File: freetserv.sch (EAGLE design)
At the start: 60 parts, among them IC2 SN75240PW, Q1 12MHz, Q2 6MHz, U1 MCP16311-E/MS, U4 TLV810SDBZT, U5 SN74LVC1G86DCKR

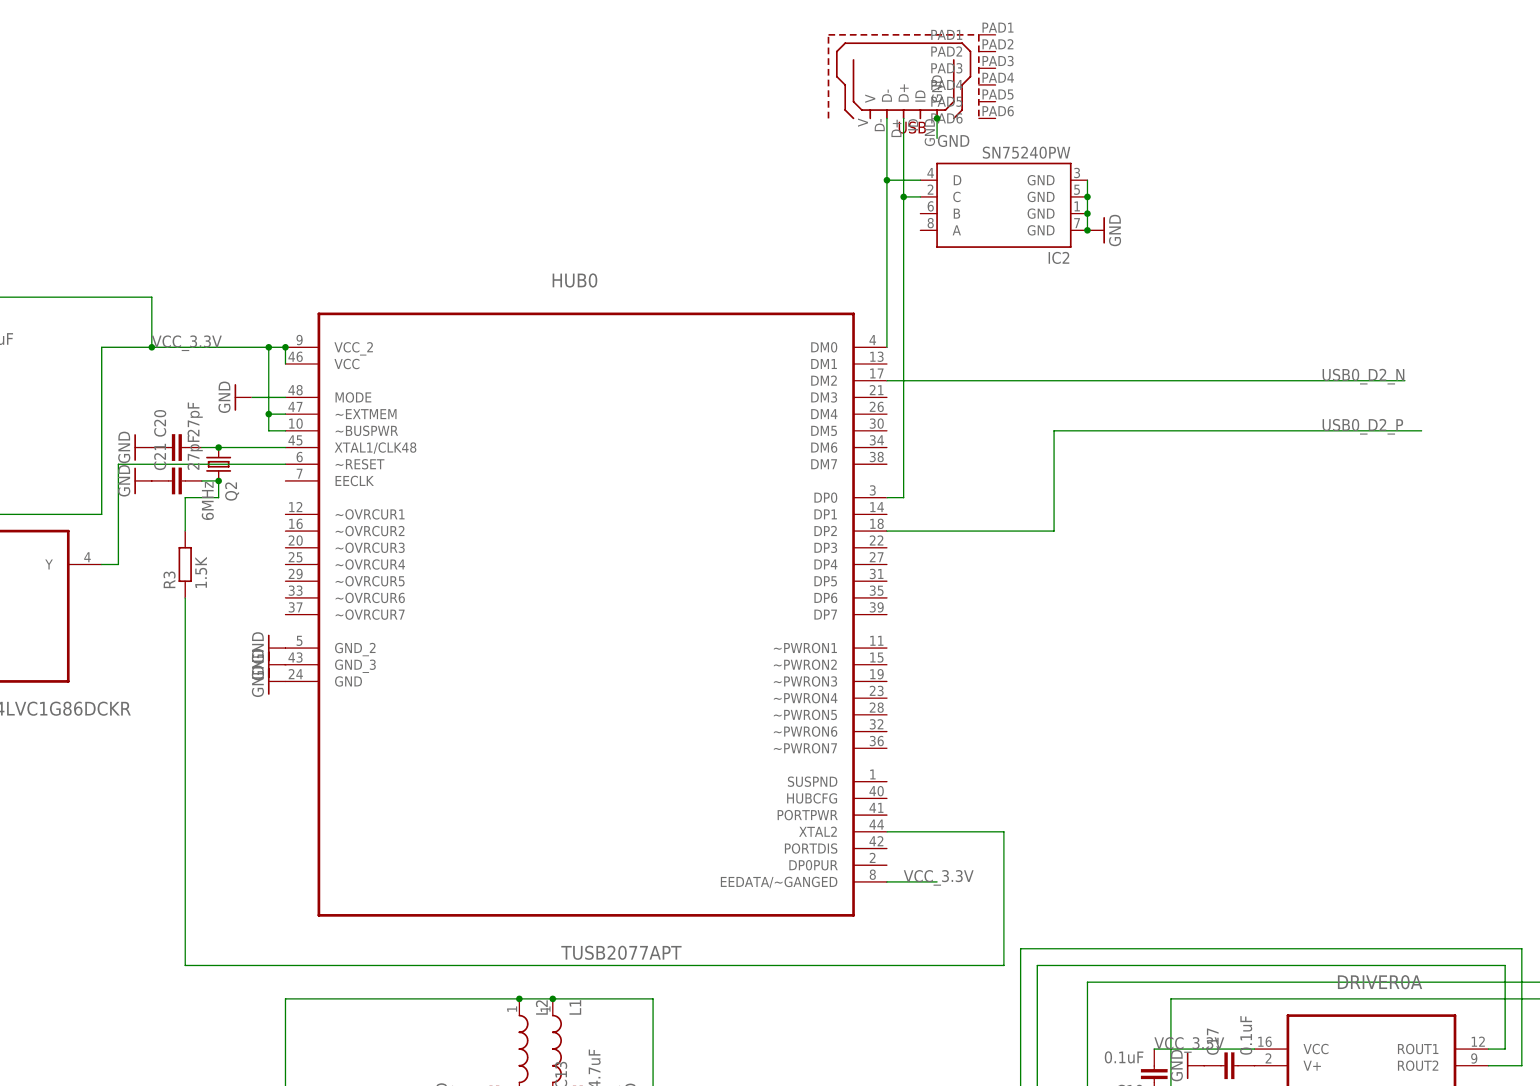
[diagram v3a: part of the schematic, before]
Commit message: use TUSB2046B (+ additional USB port), route both
Warnings need to be addressed, but the bulk of the routing should now be
done.
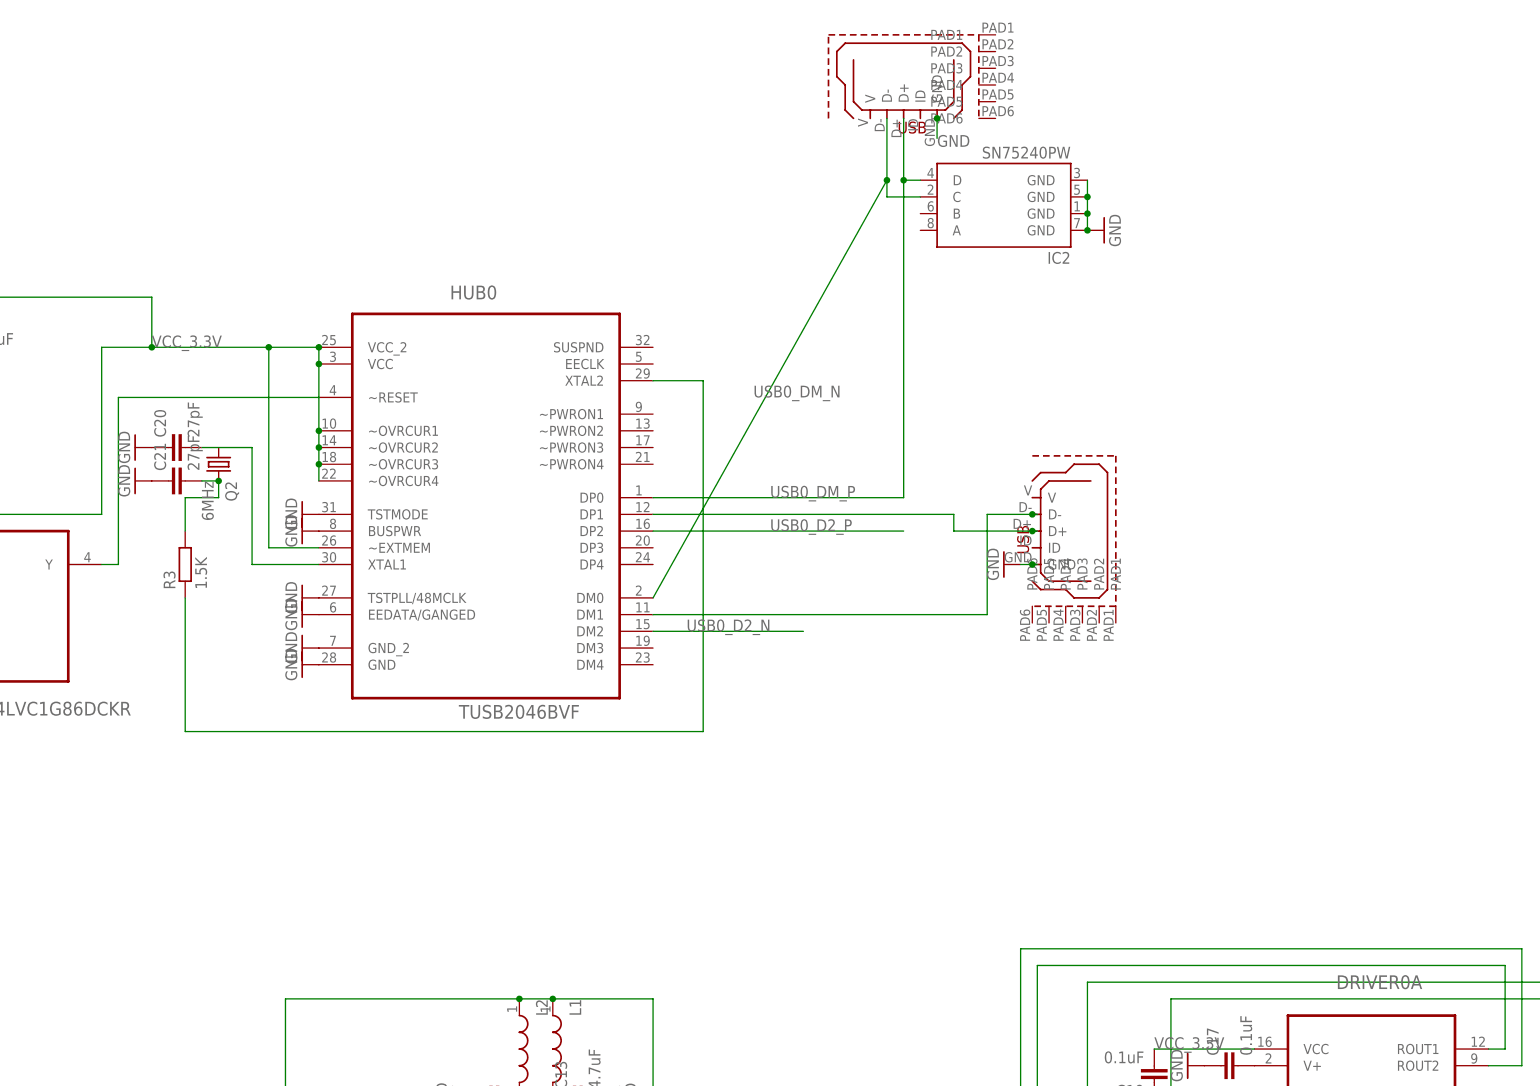
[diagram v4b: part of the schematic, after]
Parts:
- added USB_IN: USB_MICROB, ftdi_ft231xq-r:USB_MICROB
- HUB0: value TUSB2077APT -> TUSB2046BVF; device Texas Instruments_By_element14_Batch_1:TUSB2077APT -> Texas Instruments_By_element14_Batch_1:TUSB2046BVF
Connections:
- new net USB0_DM_N: HUB0.DM0, IC2.C, USB_RASPI_DATA.D-
- new net USB0_DM_P: HUB0.DP0, IC2.D, USB_RASPI_DATA.D+
- net GND: now also HUB0.BUSPWR, HUB0.EEDATA/GANGED, HUB0.TSTMODE, HUB0.TSTPLL/48MCLK, USB_IN.GND; no longer HUB0.GND_3, HUB0.MODE
- net N$1: now also HUB0.DP1, USB_IN.D+; no longer HUB0.DP0, IC2.C, USB_RASPI_DATA.D+
- net N$2: now also HUB0.DM1, USB_IN.D-; no longer HUB0.DM0, IC2.D, USB_RASPI_DATA.D-
- net N$44: now also HUB0.XTAL1; no longer HUB0.XTAL1/CLK48
- net VCC_3.3V: now also HUB0.~OVRCUR1, HUB0.~OVRCUR2, HUB0.~OVRCUR3, HUB0.~OVRCUR4; no longer HUB0.EEDATA/~GANGED, HUB0.~BUSPWR

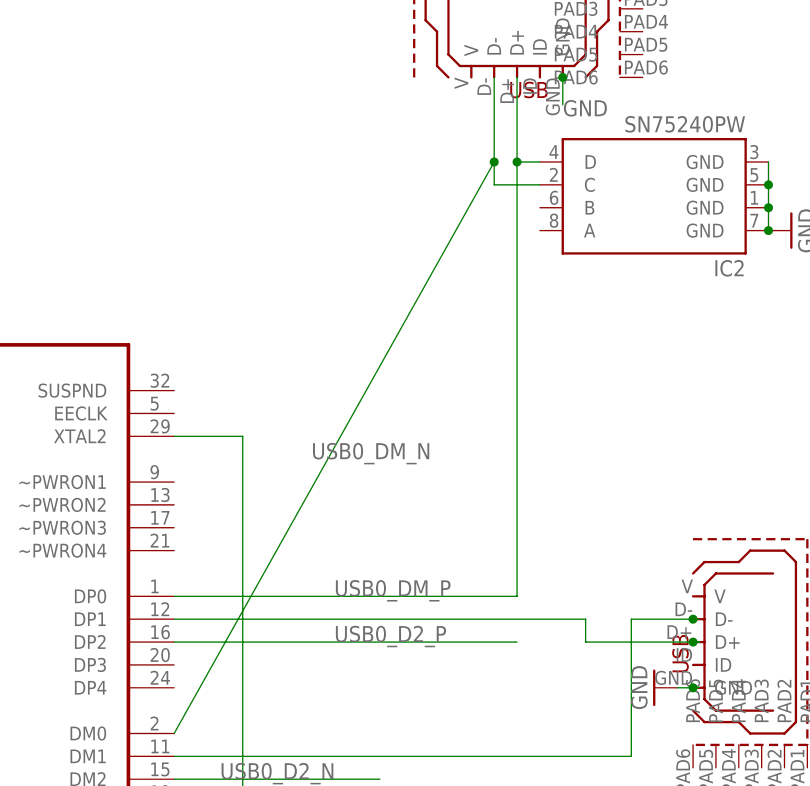
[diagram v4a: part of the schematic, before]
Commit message: hook up the second USB port to the SN75240 as well
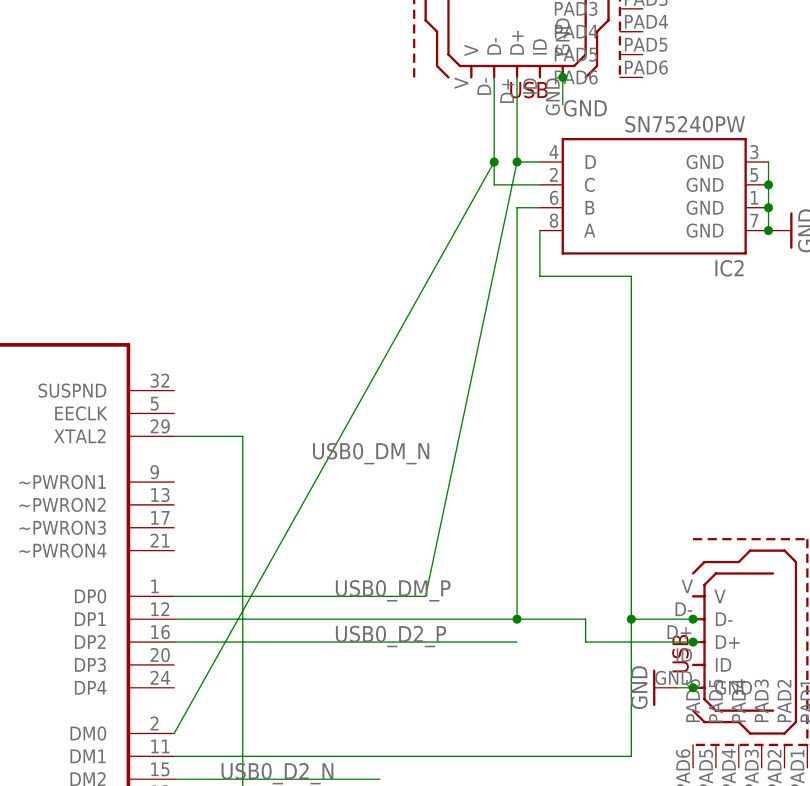
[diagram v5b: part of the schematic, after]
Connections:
- net N$1: now also IC2.B
- net N$2: now also IC2.A
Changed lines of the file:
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@@
 <pinref part="USB_RASPI_DATA" gate="G$1" pin="D+"/>
 <pinref part="HUB0" gate="A" pin="DP0"/>
-<wire x1="50.8" y1="200.66" x2="88.9" y2="200.66" width="0.1524" layer="91"/>
-<wire x1="88.9" y1="200.66" x2="88.9" y2="248.92" width="0.1524" layer="91"/>
+<wire x1="50.8" y1="200.66" x2="78.74" y2="200.66" width="0.1524" layer="91"/>
+<wire x1="78.74" y1="200.66" x2="88.9" y2="248.92" width="0.1524" layer="91"/>
 <label x="68.58" y="200.66" size="1.778" layer="95"/>
 <pinref part="IC2" gate="G$1" pin="D"/>
@@
 <wire x1="96.52" y1="195.58" x2="96.52" y2="198.12" width="0.1524" layer="91"/>
 <pinref part="HUB0" gate="A" pin="DP1"/>
-<wire x1="96.52" y1="198.12" x2="50.8" y2="198.12" width="0.1524" layer="91"/>
+<wire x1="96.52" y1="198.12" x2="88.9" y2="198.12" width="0.1524" layer="91"/>
 <pinref part="USB_IN" gate="G$1" pin="D+"/>
 <junction x="108.458" y="195.58"/>
+<pinref part="IC2" gate="G$1" pin="B"/>
+<wire x1="88.9" y1="198.12" x2="50.8" y2="198.12" width="0.1524" layer="91"/>
+<wire x1="91.44" y1="243.84" x2="88.9" y2="243.84" width="0.1524" layer="91"/>
+<wire x1="88.9" y1="243.84" x2="88.9" y2="198.12" width="0.1524" layer="91"/>
+<junction x="88.9" y="198.12"/>
 </segment>
 </net>
@@
 <pinref part="USB_IN" gate="G$1" pin="D-"/>
 <junction x="108.458" y="198.12"/>
-</segment>
-</net>
+<wire x1="101.6" y1="198.12" x2="101.6" y2="236.22" width="0.1524" layer="91"/>
+<pinref part="IC2" gate="G$1" pin="A"/>
+<wire x1="91.44" y1="241.3" x2="91.44" y2="236.22" width="0.1524" layer="91"/>
+<wire x1="91.44" y1="236.22" x2="101.6" y2="236.22" width="0.1524" layer="91"/>
+<junction x="101.6" y="198.12"/>
+</segment>
+</net>

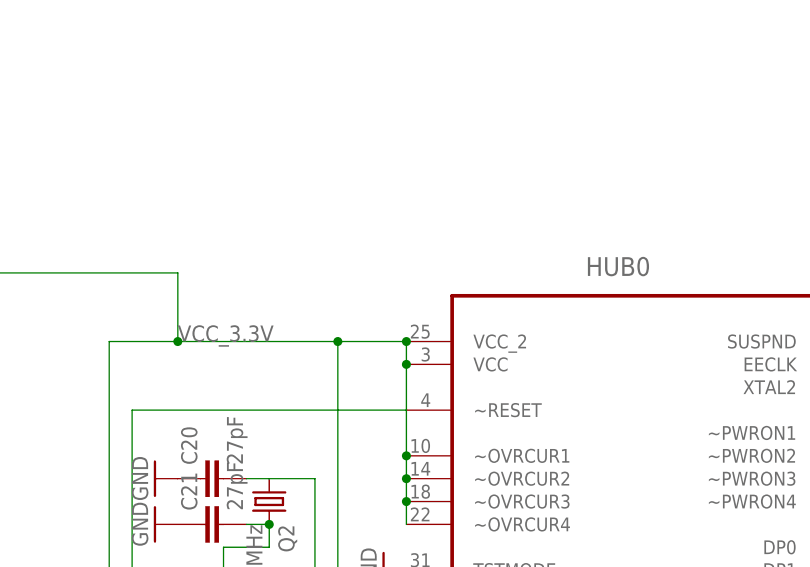
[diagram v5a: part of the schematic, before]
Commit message: make differential pairs more symmetric, move vias close to TUSB
also add the recommended 0.1uF capacitor close to the power pin
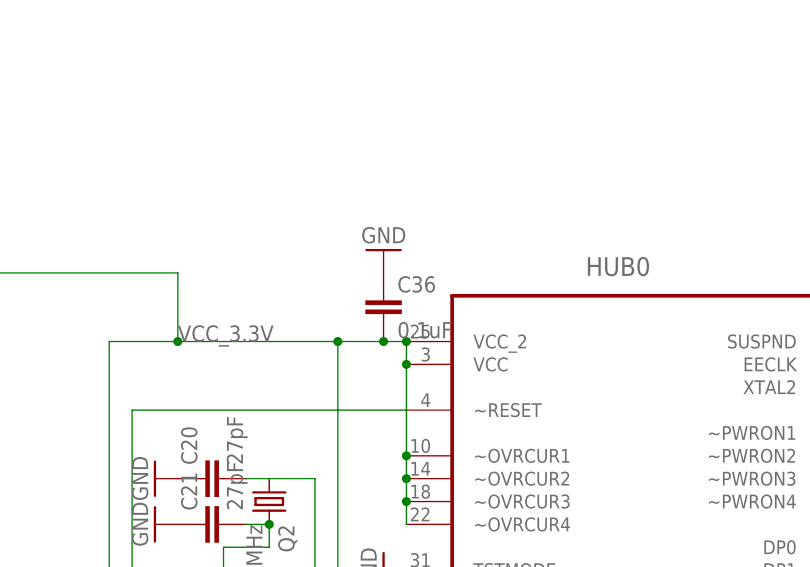
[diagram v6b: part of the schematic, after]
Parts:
- added C36: 0.1uF, resistor:C-EUC0805
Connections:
- net GND: now also C36.1
- net VCC_3.3V: now also C36.2
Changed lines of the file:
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@@
 <part name="USB_IN" library="ftdi_ft231xq-r" deviceset="USB_MICROB" device=""/>
 <part name="GND37" library="supply1" deviceset="GND" device=""/>
+<part name="C36" library="resistor" deviceset="C-EU" device="C0805" value="0.1uF"/>
+<part name="GND42" library="supply1" deviceset="GND" device=""/>
 </parts>
 <sheets>
@@
 <instance part="USB_IN" gate="G$1" x="108.458" y="194.31" rot="MR0"/>
 <instance part="GND37" gate="1" x="104.14" y="190.5" rot="R270"/>
+<instance part="C36" gate="G$1" x="-2.54" y="228.6"/>
+<instance part="GND42" gate="1" x="-2.54" y="233.68" rot="R180"/>
 </instances>
 <busses>
@@
 <junction x="108.458" y="190.5"/>
 </segment>
+<segment>
+<pinref part="C36" gate="G$1" pin="1"/>
+<pinref part="GND42" gate="1" pin="GND"/>
+</segment>
 </net>
 <net name="USB0_DM_P" class="0">
@@
 <wire x1="0" y1="223.52" x2="0" y2="220.98" width="0.1524" layer="91"/>
 <junction x="0" y="223.52"/>
-<wire x1="-7.62" y1="223.52" x2="0" y2="223.52" width="0.1524" layer="91"/>
+<wire x1="-7.62" y1="223.52" x2="-2.54" y2="223.52" width="0.1524" layer="91"/>
 <junction x="-7.62" y="223.52"/>
 <pinref part="HUB0" gate="A" pin="~EXTMEM"/>
+<wire x1="-2.54" y1="223.52" x2="0" y2="223.52" width="0.1524" layer="91"/>
 <wire x1="0" y1="193.04" x2="-7.62" y2="193.04" width="0.1524" layer="91"/>
 <wire x1="-7.62" y1="193.04" x2="-7.62" y2="223.52" width="0.1524" layer="91"/>
@@
 <junction x="0" y="205.74"/>
 <wire x1="0" y1="205.74" x2="0" y2="203.2" width="0.1524" layer="91"/>
-</segment>
-<segment>
+<pinref part="C36" gate="G$1" pin="2"/>
+<junction x="-2.54" y="223.52"/>
+</segment>
+<segment>

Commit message: address all DRC warnings
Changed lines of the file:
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@@
 <clearance class="1" value="0.2"/>
 </class>
-<class number="2" name="power" width="1.143" drill="0">
+<class number="2" name="power" width="0.4064" drill="0">
 </class>
 </classes>
@@
 <part name="C36" library="resistor" deviceset="C-EU" device="C0805" value="0.1uF"/>
 <part name="GND42" library="supply1" deviceset="GND" device=""/>
+<part name="GND43" library="supply1" deviceset="GND" device=""/>
+<part name="GND48" library="supply1" deviceset="GND" device=""/>
+<part name="GND49" library="supply1" deviceset="GND" device=""/>
 </parts>
 <sheets>
@@
 <instance part="C36" gate="G$1" x="-2.54" y="228.6"/>
 <instance part="GND42" gate="1" x="-2.54" y="233.68" rot="R180"/>
+<instance part="GND43" gate="1" x="119.38" y="248.92" rot="R90"/>
+<instance part="GND48" gate="1" x="119.38" y="246.38" rot="R90"/>
+<instance part="GND49" gate="1" x="119.38" y="243.84" rot="R90"/>
 </instances>
 <busses>
@@
 <pinref part="IC2" gate="G$1" pin="GND@1"/>
 <pinref part="GND8" gate="1" pin="GND"/>
-<pinref part="IC2" gate="G$1" pin="GND@4"/>
-<wire x1="116.84" y1="248.92" x2="116.84" y2="246.38" width="0.1524" layer="91"/>
-<pinref part="IC2" gate="G$1" pin="GND@2"/>
-<junction x="116.84" y="243.84"/>
-<wire x1="116.84" y1="246.38" x2="116.84" y2="243.84" width="0.1524" layer="91"/>
-<wire x1="116.84" y1="243.84" x2="116.84" y2="241.3" width="0.1524" layer="91"/>
-<pinref part="IC2" gate="G$1" pin="GND@3"/>
-<junction x="116.84" y="246.38"/>
-<junction x="116.84" y="241.3"/>
 </segment>
 <segment>
@@
 <pinref part="GND42" gate="1" pin="GND"/>
 </segment>
+<segment>
+<pinref part="IC2" gate="G$1" pin="GND@4"/>
+<pinref part="GND43" gate="1" pin="GND"/>
+</segment>
+<segment>
+<pinref part="IC2" gate="G$1" pin="GND@3"/>
+<pinref part="GND48" gate="1" pin="GND"/>
+</segment>
+<segment>
+<pinref part="IC2" gate="G$1" pin="GND@2"/>
+<pinref part="GND49" gate="1" pin="GND"/>
+</segment>
 </net>

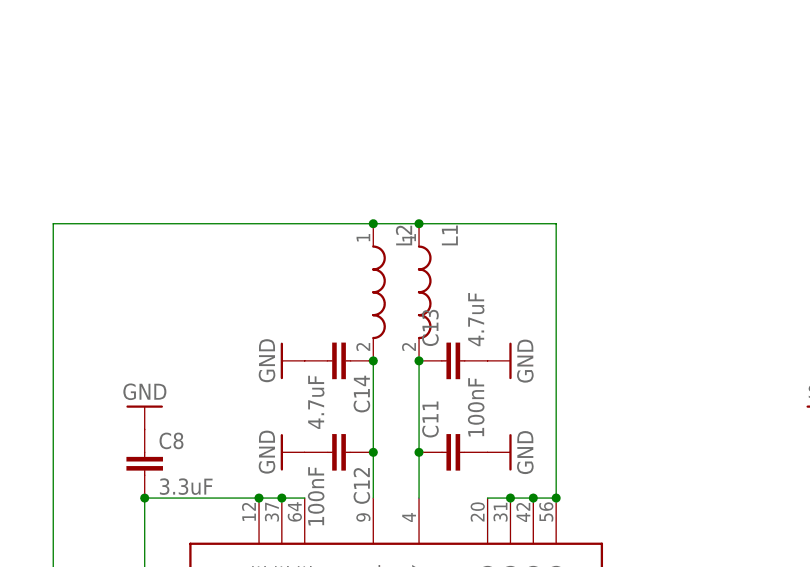
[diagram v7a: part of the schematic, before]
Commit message: renamed L1, L2 to FERRITE1, FERRITE2, added values
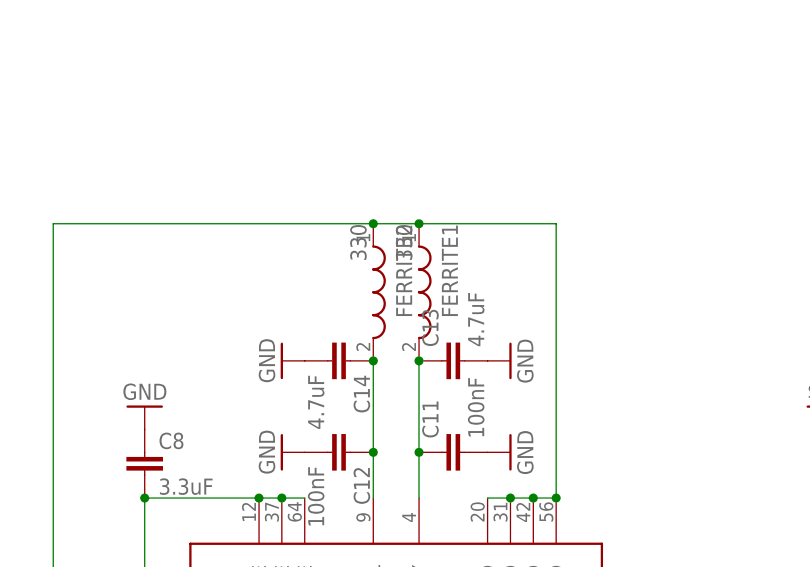
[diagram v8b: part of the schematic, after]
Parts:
- FERRITE1, FERRITE2: value (none) -> 330
- renumbered L1 to FERRITE1, L2 to FERRITE2
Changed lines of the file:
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@@
 <?xml version="1.0" encoding="utf-8"?>
 <!DOCTYPE eagle SYSTEM "eagle.dtd">
-<eagle version="7.3.0">
+<eagle version="7.4.0">
 <drawing>
 <settings>
@@
 <part name="GND19" library="supply1" deviceset="GND" device=""/>
 <part name="GND20" library="supply1" deviceset="GND" device=""/>
-<part name="L1" library="Wurth_Elektronik_Passive_rev15d" deviceset="WE-KI" device="_0805A"/>
-<part name="L2" library="Wurth_Elektronik_Passive_rev15d" deviceset="WE-KI" device="_0805A"/>
+<part name="FERRITE1" library="Wurth_Elektronik_Passive_rev15d" deviceset="WE-KI" device="_0805A" value="330"/>
+<part name="FERRITE2" library="Wurth_Elektronik_Passive_rev15d" deviceset="WE-KI" device="_0805A" value="330"/>
 <part name="C11" library="resistor" deviceset="C-EU" device="C0805" value="100nF"/>
 <part name="C12" library="resistor" deviceset="C-EU" device="C0805" value="100nF"/>
@@
 <instance part="GND19" gate="1" x="63.5" y="55.88" rot="R90"/>
 <instance part="GND20" gate="1" x="63.5" y="50.8" rot="R90"/>
-<instance part="L1" gate="G$1" x="35.56" y="116.84" rot="R270"/>
-<instance part="L2" gate="G$1" x="30.48" y="116.84" rot="R270"/>
+<instance part="FERRITE1" gate="G$1" x="35.56" y="116.84" rot="R270"/>
+<instance part="FERRITE2" gate="G$1" x="30.48" y="116.84" rot="R270"/>
 <instance part="C11" gate="G$1" x="38.1" y="99.06" rot="R90"/>
 <instance part="C12" gate="G$1" x="27.94" y="99.06" rot="R270"/>
@@
 <net name="N$17" class="0">
 <segment>
-<pinref part="L1" gate="G$1" pin="2"/>
+<pinref part="FERRITE1" gate="G$1" pin="2"/>
 <pinref part="SERIAL0" gate="CORE" pin="VPHY"/>
 <pinref part="C11" gate="G$1" pin="1"/>
@@
 <segment>
 <pinref part="SERIAL0" gate="CORE" pin="VPLL"/>
-<pinref part="L2" gate="G$1" pin="2"/>
+<pinref part="FERRITE2" gate="G$1" pin="2"/>
 <wire x1="30.48" y1="93.98" x2="30.48" y2="99.06" width="0.1524" layer="91"/>
 <pinref part="C12" gate="G$1" pin="1"/>
@@
 <junction x="48.26" y="93.98"/>
 <junction x="50.8" y="93.98"/>
-<pinref part="L2" gate="G$1" pin="1"/>
-<pinref part="L1" gate="G$1" pin="1"/>
+<pinref part="FERRITE2" gate="G$1" pin="1"/>
+<pinref part="FERRITE1" gate="G$1" pin="1"/>
 <junction x="35.56" y="124.46"/>
 <junction x="30.48" y="124.46"/>
